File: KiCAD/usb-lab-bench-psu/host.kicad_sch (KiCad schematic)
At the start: 29 parts, among them J4 USB_C_Receptacle, SW2 SW_Push, U2 USBLC6-2SC6, U3 ESP32-C3, U4 ZD25WQ32C, Y1 40MHz

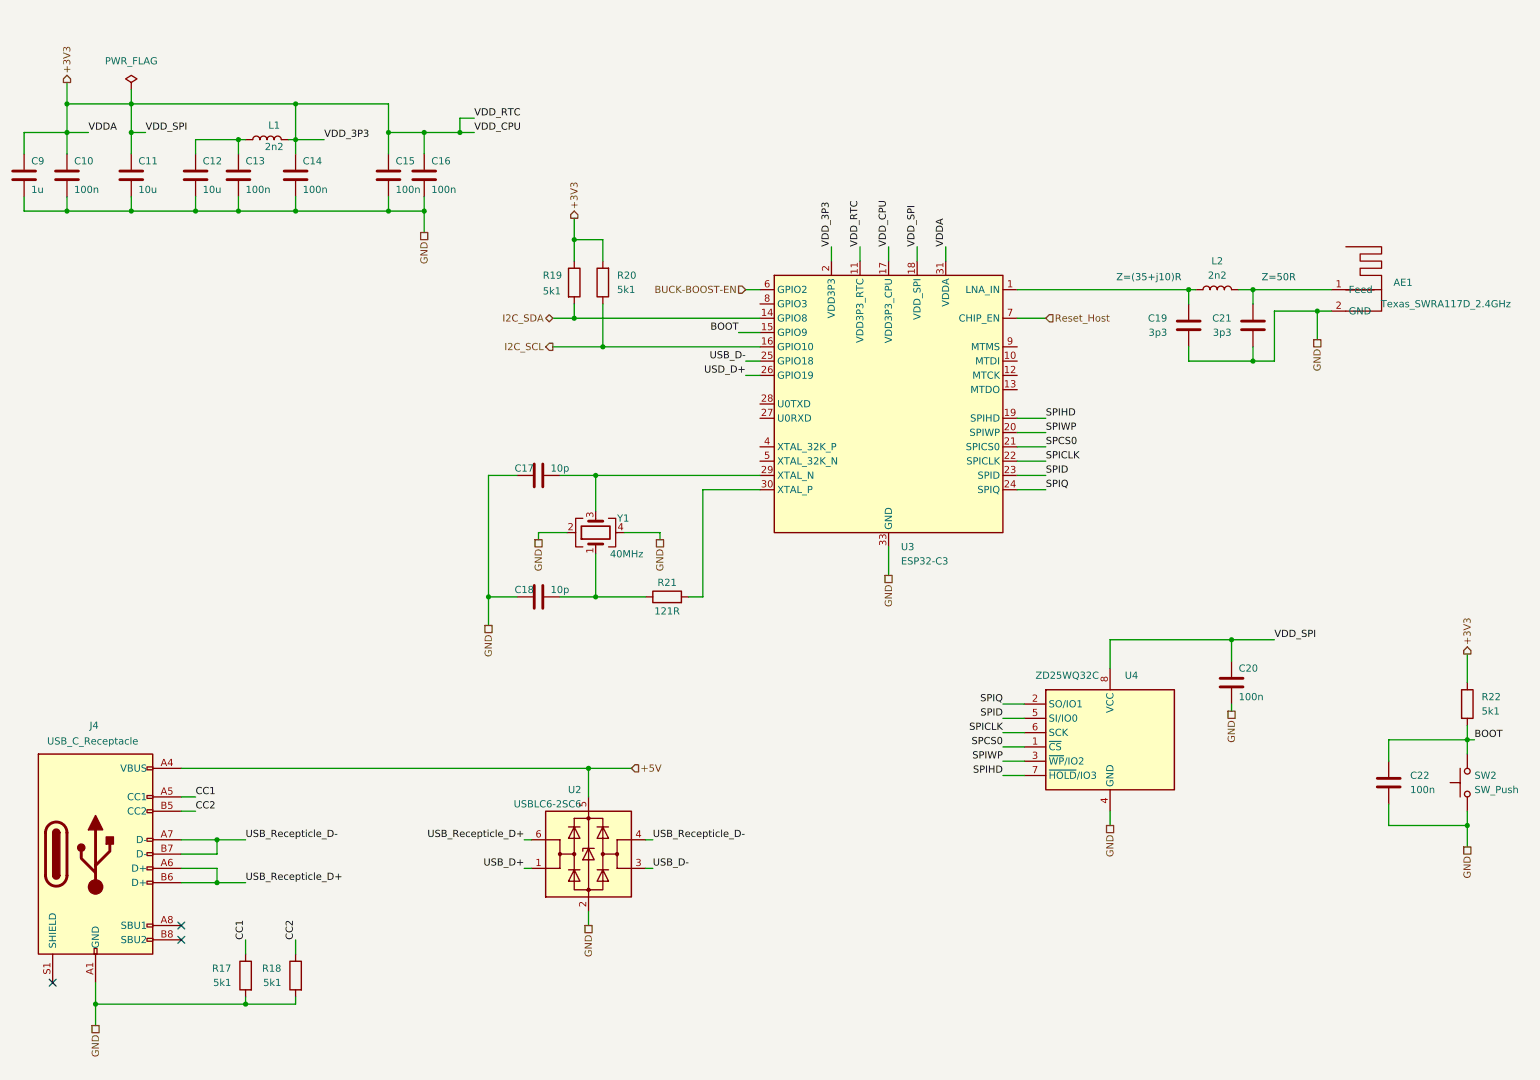
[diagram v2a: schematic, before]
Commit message: adapted buck converter
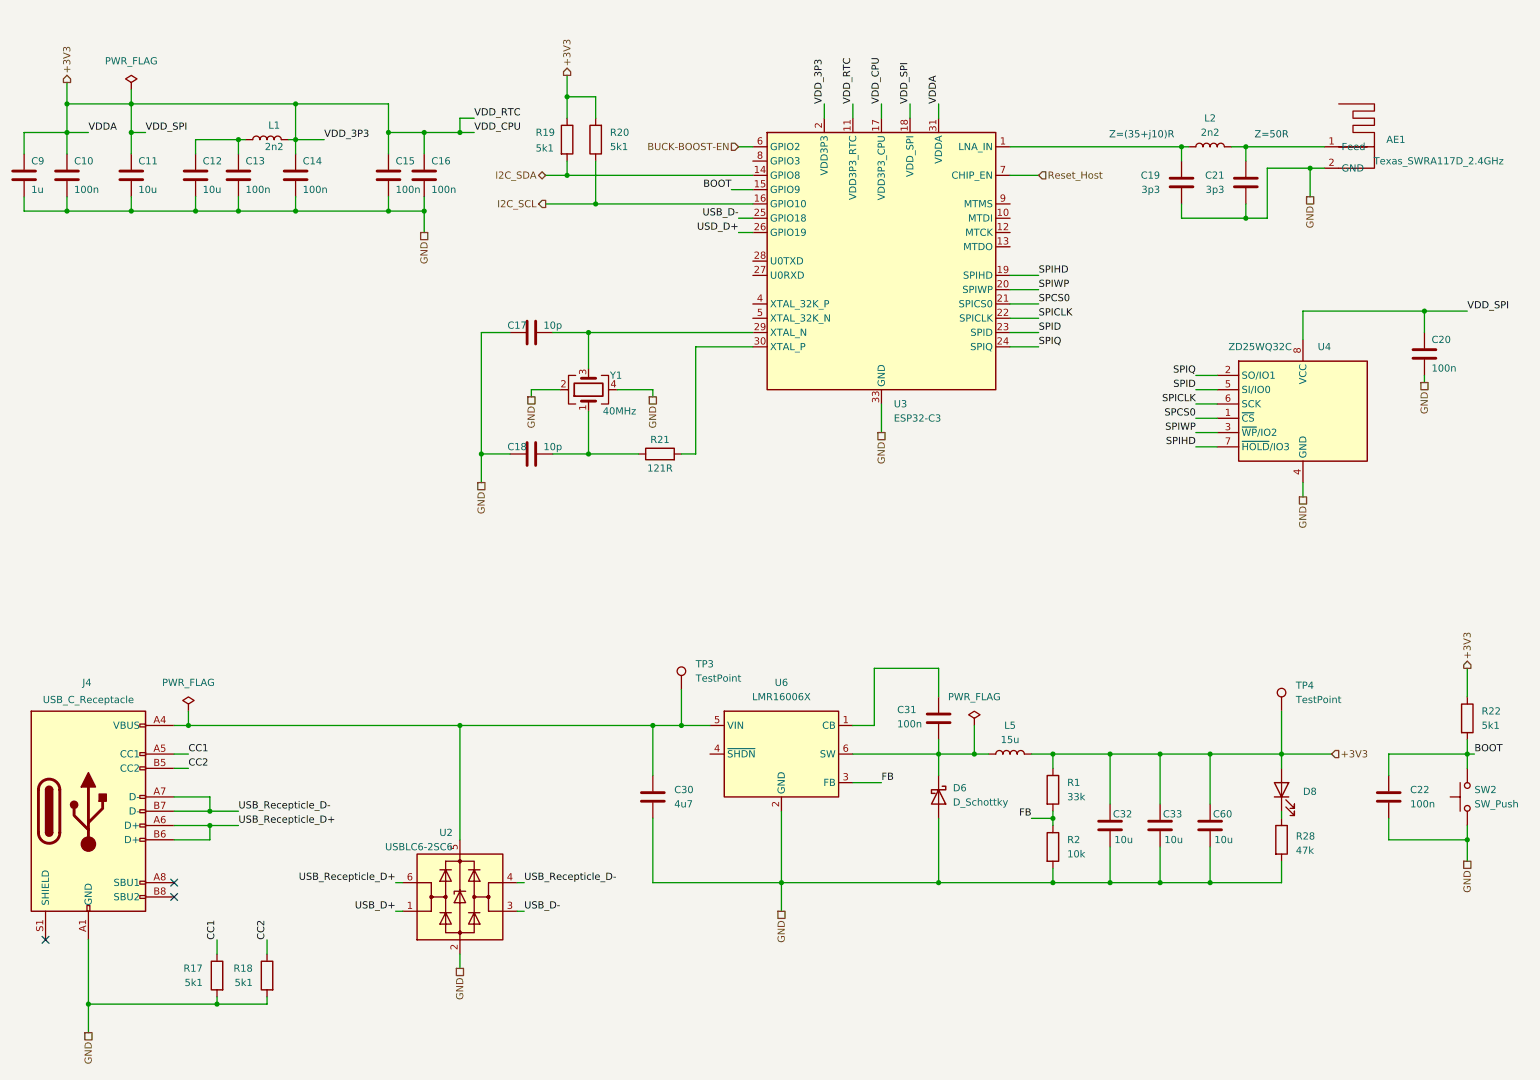
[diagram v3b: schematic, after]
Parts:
- added C30: 4u7, symbol Device:C
- added C31: 100n, symbol Device:C
- added C32, C33, C60: 10u, symbol Device:C
- added D6: D_Schottky, symbol Device:D_Schottky
- added D8: XL-1005UGC, Diode_SMD:D_0402_1005Metric_Pad0.77x0.64mm_HandSolder, symbol Device:LED
- added L5: 15u, symbol Device:L
- added R1: 33k, Resistor_SMD:R_0402_1005Metric_Pad0.72x0.64mm_HandSolder, symbol Device:R
- added R2: 10k, Resistor_SMD:R_0402_1005Metric_Pad0.72x0.64mm_HandSolder, symbol Device:R
- added R28: 47k, Resistor_SMD:R_0402_1005Metric_Pad0.72x0.64mm_HandSolder, symbol Device:R
- added TP3, TP4: TestPoint, symbol Connector:TestPoint
- added U6: LMR16006X, Package_TO_SOT_SMD:TSOT-23-6, symbol Prj_dcdc_converter:LMR16006X
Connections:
- net +3V3: now also C32.1, C33.1, C60.1, D8.2 (A), L5.2, R1.1, TP4.1
- net GND: now also C30.2, C32.2, C33.2, C60.2, D6.2 (A), R2.2, R28.2, U6.2 (GND)
- net +5V: no longer names the net of J4.A4 (VBUS), J4.A9 (VBUS), J4.B4 (VBUS), J4.B9 (VBUS), U2.5 (VBUS)
- net +5V: now also C30.1, TP3.1, U6.5 (VIN)
- new net: C31.2, D6.1 (K), L5.1, U6.6 (SW)
- new net: D8.1 (K), R28.1
- new net: C31.1, U6.1 (CB)
- new net FB: R1.2, R2.1, U6.3 (FB)
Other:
- moved on the sheet: AE1, C17, C18, C19, C20, C21, C22, J4, L2, R17, R18, R19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

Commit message: restructured schematics to better show individual boards
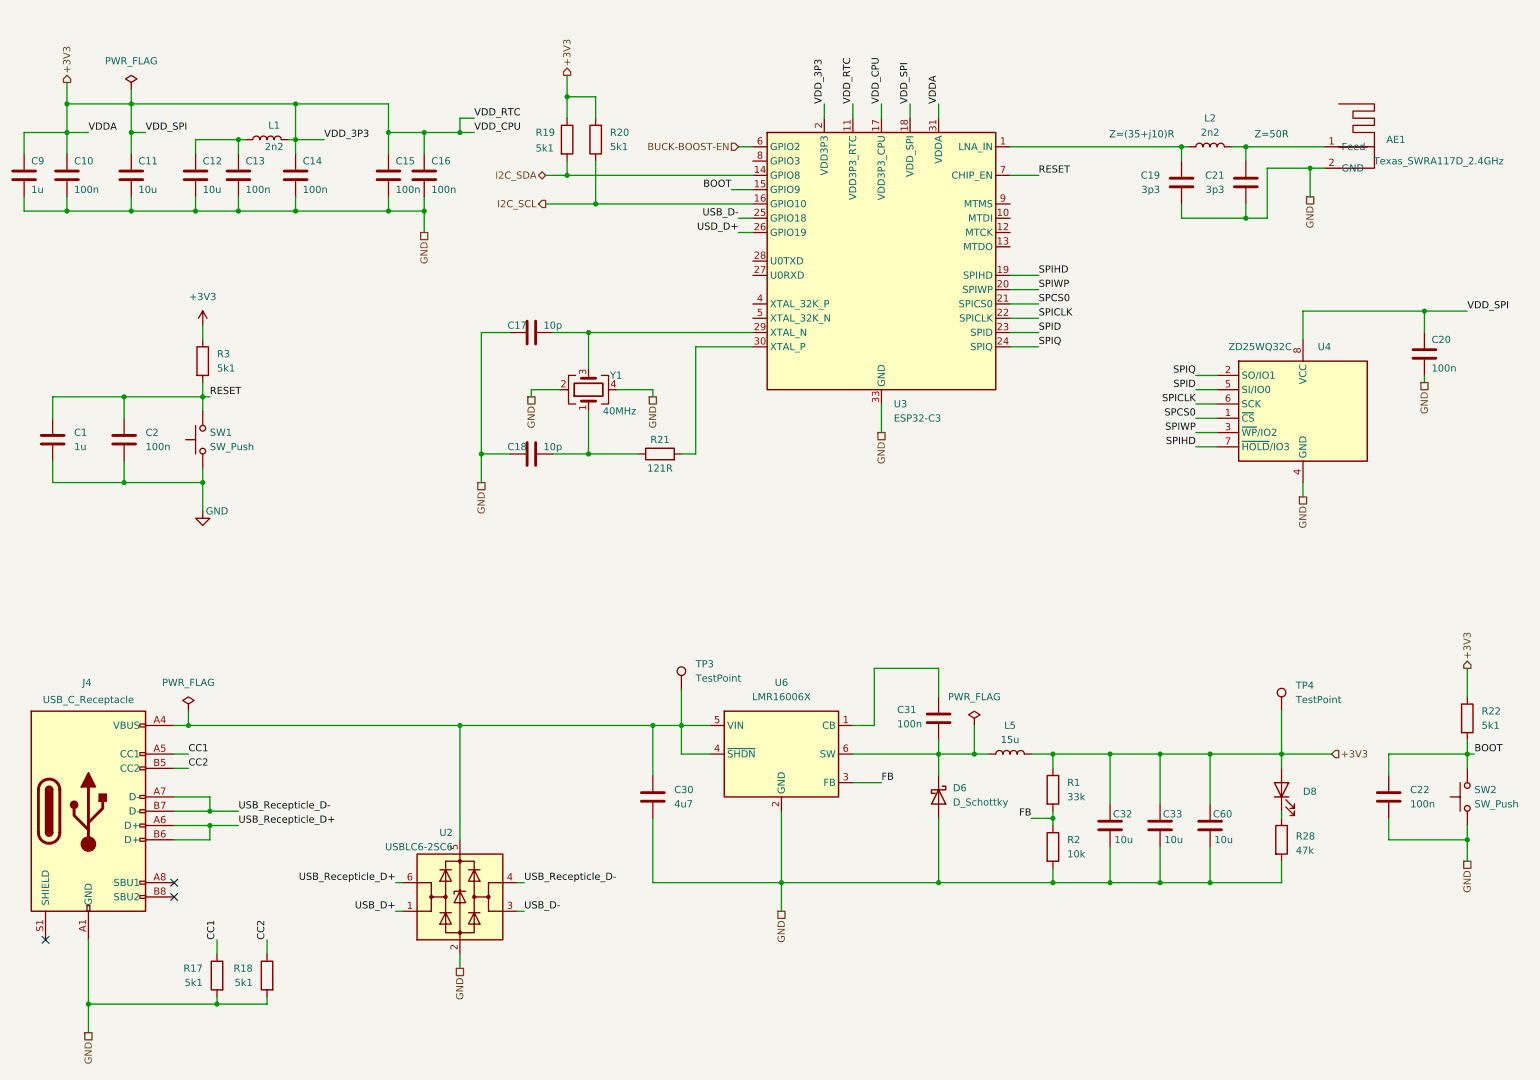
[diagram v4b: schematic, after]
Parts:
- added C1: 1u, Capacitor_SMD:C_0402_1005Metric_Pad0.74x0.62mm_HandSolder, symbol Device:C
- added C2: 100n, Capacitor_SMD:C_0402_1005Metric_Pad0.74x0.62mm_HandSolder, symbol Device:C
- added R3: 5k1, Resistor_SMD:R_0402_1005Metric_Pad0.72x0.64mm_HandSolder, symbol Device:R
- added SW1: SW_Push, Button_Switch_SMD:SW_SPST_TL3342, symbol Switch:SW_Push
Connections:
- net +3V3: now also R3.1
- net GND: now also C1.2, C2.2, SW1.1
- net at C30.1, J4.A4 (VBUS), J4.A9 (VBUS)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: now also U6.4 (~{SHDN})
- net Reset_Host renamed RESET
- net RESET: now also C1.1, C2.1, R3.2, SW1.2

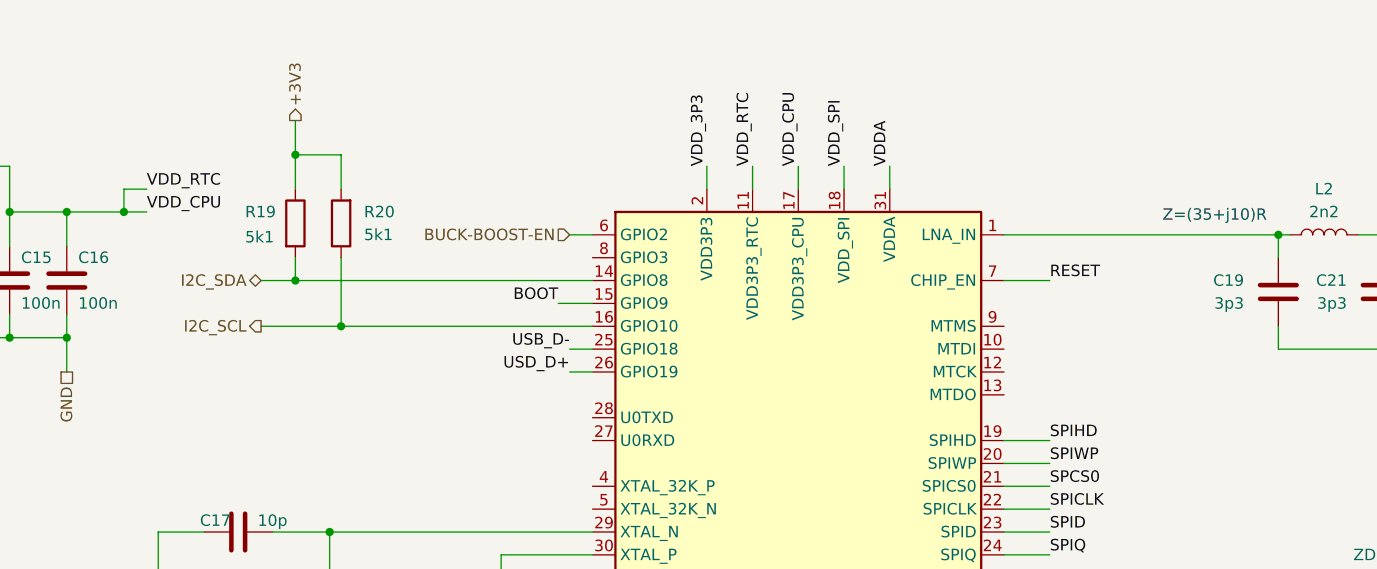
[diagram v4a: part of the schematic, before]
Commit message: updated spi for display
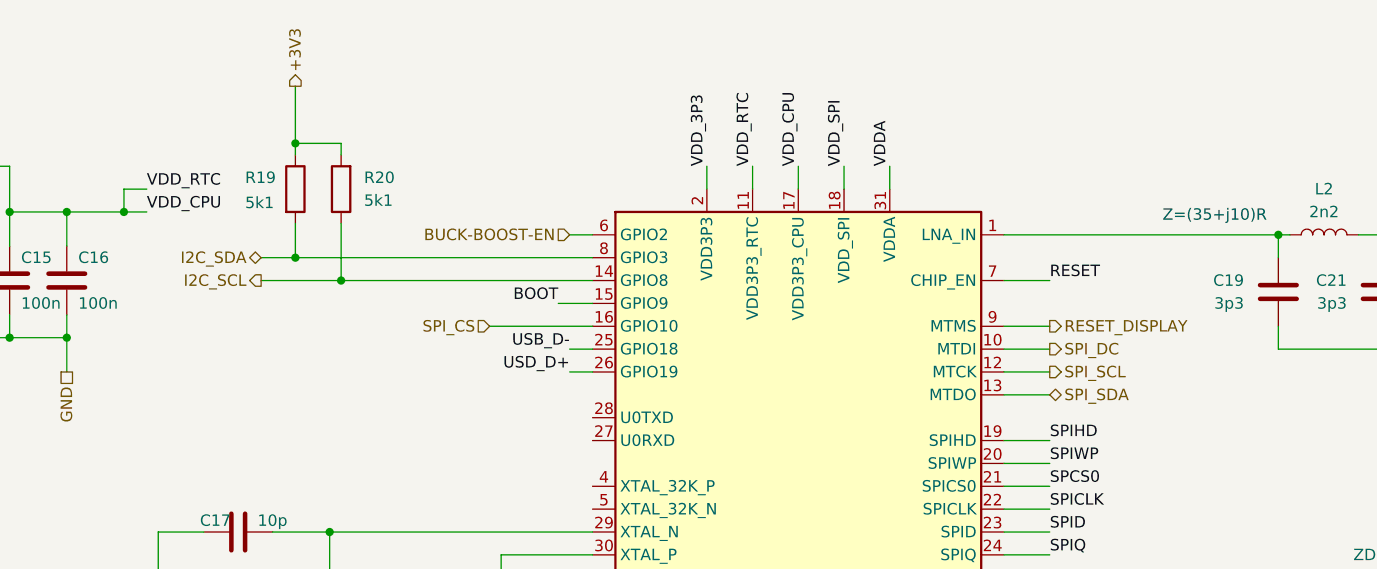
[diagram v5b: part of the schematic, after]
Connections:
- net I2C_SCL: now also U3.14 (GPIO8); no longer U3.16 (GPIO10)
- net I2C_SDA: now also U3.8 (GPIO3); no longer U3.14 (GPIO8)
- net SPI_DC: now reaches U3.10 (MTDI)
- net SPI_SCL: now reaches U3.12 (MTCK)
- net SPI_SDA: now reaches U3.13 (MTDO)
- net RESET_DISPLAY: now reaches U3.9 (MTMS)
- new net SPI_CS: U3.16 (GPIO10)
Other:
- moved on the sheet: R19, R20
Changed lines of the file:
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@@
 	)
 	(junction
-		(at 113.03 24.13)
-		(diameter 0)
-		(color 0 0 0 0)
-	)
-	(junction
 		(at 27.94 185.42)
 		(diameter 0)
@@
 	)
 	(junction
+		(at 113.03 35.56)
+		(diameter 0)
+		(color 0 0 0 0)
+	)
+	(junction
 		(at 87.63 44.45)
 		(diameter 0)
@@
 	)
 	(junction
-		(at 118.11 43.18)
+		(at 118.11 38.1)
 		(diameter 0)
 		(color 0 0 0 0)
@@
 	)
 	(junction
-		(at 24.13 25.4)
+		(at 113.03 22.86)
 		(diameter 0)
 		(color 0 0 0 0)
 	)
 	(junction
-		(at 113.03 38.1)
+		(at 24.13 25.4)
 		(diameter 0)
 		(color 0 0 0 0)
@@
 	(wire
 		(pts
+			(xy 113.03 22.86) (xy 113.03 24.13)
+		)
+		(stroke
+			(width 0)
+			(type default)
+		)
+	)
+	(wire
+		(pts
 			(xy 223.52 33.02) (xy 222.25 33.02)
 		)
@@
 	(wire
 		(pts
-			(xy 113.03 20.32) (xy 113.03 24.13)
+			(xy 134.62 43.18) (xy 146.05 43.18)
 		)
 		(stroke
@@
 	(wire
 		(pts
-			(xy 21.59 81.28) (xy 21.59 77.47)
+			(xy 113.03 16.51) (xy 113.03 22.86)
 		)
 		(stroke
@@
 	(wire
 		(pts
-			(xy 168.91 78.74) (xy 168.91 83.82)
+			(xy 21.59 81.28) (xy 21.59 77.47)
 		)
 		(stroke
@@
 	(wire
 		(pts
-			(xy 49.53 151.13) (xy 49.53 148.59)
+			(xy 168.91 78.74) (xy 168.91 83.82)
 		)
 		(stroke
@@
 	(wire
 		(pts
-			(xy 34.29 92.71) (xy 48.26 92.71)
+			(xy 49.53 151.13) (xy 49.53 148.59)
 		)
 		(stroke
@@
 	(wire
 		(pts
-			(xy 243.84 62.23) (xy 265.43 62.23)
+			(xy 34.29 92.71) (xy 48.26 92.71)
 		)
 		(stroke
@@
 	(wire
 		(pts
-			(xy 113.03 24.13) (xy 113.03 27.94)
+			(xy 243.84 62.23) (xy 265.43 62.23)
 		)
 		(stroke
@@
 	(wire
 		(pts
+			(xy 191.77 50.8) (xy 196.85 50.8)
+		)
+		(stroke
+			(width 0)
+			(type default)
+		)
+	)
+	(wire
+		(pts
 			(xy 273.05 156.21) (xy 273.05 160.02)
 		)
@@
 	(wire
 		(pts
-			(xy 118.11 35.56) (xy 118.11 43.18)
+			(xy 118.11 31.75) (xy 118.11 38.1)
 		)
 		(stroke
@@
 	(wire
 		(pts
-			(xy 118.11 43.18) (xy 146.05 43.18)
+			(xy 118.11 38.1) (xy 146.05 38.1)
 		)
 		(stroke
@@
 	(wire
 		(pts
+			(xy 191.77 48.26) (xy 196.85 48.26)
+		)
+		(stroke
+			(width 0)
+			(type default)
+		)
+	)
+	(wire
+		(pts
 			(xy 224.79 73.66) (xy 228.6 73.66)
 		)
@@
 	(wire
 		(pts
-			(xy 113.03 38.1) (xy 146.05 38.1)
+			(xy 113.03 35.56) (xy 146.05 35.56)
 		)
 		(stroke
@@
 	(wire
 		(pts
-			(xy 109.22 43.18) (xy 118.11 43.18)
+			(xy 109.22 38.1) (xy 118.11 38.1)
 		)
 		(stroke
@@
 	(wire
 		(pts
-			(xy 118.11 24.13) (xy 113.03 24.13)
+			(xy 118.11 22.86) (xy 113.03 22.86)
 		)
 		(stroke
@@
 	(wire
 		(pts
+			(xy 191.77 43.18) (xy 196.85 43.18)
+		)
+		(stroke
+			(width 0)
+			(type default)
+		)
+	)
+	(wire
+		(pts
 			(xy 133.35 87.63) (xy 135.89 87.63)
 		)
@@
 	(wire
 		(pts
+			(xy 191.77 45.72) (xy 196.85 45.72)
+		)
+		(stroke
+			(width 0)
+			(type default)
+		)
+	)
+	(wire
+		(pts
 			(xy 224.79 81.28) (xy 228.6 81.28)
 		)
@@
 	(wire
 		(pts
-			(xy 109.22 38.1) (xy 113.03 38.1)
+			(xy 109.22 35.56) (xy 113.03 35.56)
 		)
 		(stroke
@@
 	(wire
 		(pts
-			(xy 113.03 35.56) (xy 113.03 38.1)
+			(xy 113.03 31.75) (xy 113.03 35.56)
 		)
 		(stroke
@@
 	(wire
 		(pts
-			(xy 118.11 27.94) (xy 118.11 24.13)
+			(xy 118.11 24.13) (xy 118.11 22.86)
 		)
 		(stroke
@@
 		)
 	)
+	(hierarchical_label "SPI_SCL"
+		(shape output)
+		(at 196.85 48.26 0)
+		(effects
+			(font
+				(size 1.27 1.27)
+			)
+			(justify left)
+		)
+	)
 	(hierarchical_label "I2C_SCL"
 		(shape output)
-		(at 109.22 43.18 180)
+		(at 109.22 38.1 180)
+		(effects
+			(font
+				(size 1.27 1.27)
+			)
+			(justify right)
+		)
+	)
+	(hierarchical_label "SPI_CS"
+		(shape input)
+		(at 134.62 43.18 180)
 		(effects
 			(font
@@
 	(hierarchical_label "+3V3"
 		(shape output)
-		(at 113.03 20.32 90)
+		(at 113.03 16.51 90)
 		(effects
 			(font
@@
 		)
 	)
+	(hierarchical_label "RESET_DISPLAY"
+		(shape output)
+		(at 196.85 43.18 0)
+		(effects
+			(font
+				(size 1.27 1.27)
+			)
+			(justify left)
+		)
+	)
 	(hierarchical_label "GND"
 		(shape passive)
@@
 	(hierarchical_label "I2C_SDA"
 		(shape bidirectional)
-		(at 109.22 38.1 180)
+		(at 109.22 35.56 180)
 		(effects
 			(font
@@
 		)
 	)
+	(hierarchical_label "SPI_SDA"
+		(shape bidirectional)
+		(at 196.85 50.8 0)
+		(effects
+			(font
+				(size 1.27 1.27)
+			)
+			(justify left)
+		)
+	)
+	(hierarchical_label "SPI_DC"
+		(shape output)
+		(at 196.85 45.72 0)
+		(effects
+			(font
+				(size 1.27 1.27)
+			)
+			(justify left)
+		)
+	)
 	(hierarchical_label "GND"
 		(shape passive)
@@
 	(symbol
 		(lib_id "Device:R")
-		(at 113.03 31.75 0)
+		(at 113.03 27.94 0)
 		(unit 1)
 		(exclude_from_sim no)
@@
 		(dnp no)
 		(property "Reference" "R19"
-			(at 107.442 30.48 0)
+			(at 107.442 26.67 0)
 			(effects
 				(font
@@
 		)
 		(property "Value" "5k1"
-			(at 107.442 33.274 0)
+			(at 107.442 29.464 0)
 			(effects
 				(font
@@
 		)
 		(property "Footprint" ""
-			(at 111.252 31.75 90)
+			(at 111.252 27.94 90)
 			(effects
 				(font
@@
 		)
 		(property "Datasheet" "~"
-			(at 113.03 31.75 0)
+			(at 113.03 27.94 0)
 			(effects
 				(font
@@
 		)
 		(property "Description" "Resistor"
-			(at 113.03 31.75 0)
+			(at 113.03 27.94 0)
 			(effects
 				(font
@@
 	(symbol
 		(lib_id "Device:R")
-		(at 118.11 31.75 180)
+		(at 118.11 27.94 180)
 		(unit 1)
 		(exclude_from_sim no)
@@
 		(fields_autoplaced yes)
 		(property "Reference" "R20"
-			(at 120.65 30.4799 0)
+			(at 120.65 26.6699 0)
 			(effects
 				(font
@@
 		)
 		(property "Value" "5k1"
-			(at 120.65 33.0199 0)
+			(at 120.65 29.2099 0)
 			(effects
 				(font
@@
 		)
 		(property "Footprint" ""
-			(at 119.888 31.75 90)
+			(at 119.888 27.94 90)
 			(effects
 				(font
@@
 		)
 		(property "Datasheet" "~"
-			(at 118.11 31.75 0)
+			(at 118.11 27.94 0)
 			(effects
 				(font
@@
 		)
 		(property "Description" "Resistor"
-			(at 118.11 31.75 0)
+			(at 118.11 27.94 0)
 			(effects
 				(font
